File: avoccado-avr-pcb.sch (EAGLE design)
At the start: 31 parts, among them IC1 MCP1703CB, Q1 #MHz, Q2 MOSFET-NCHANNEL2N7002PW, U1 ATMEGA168#, U2 MCP73831, X1 Micro USB

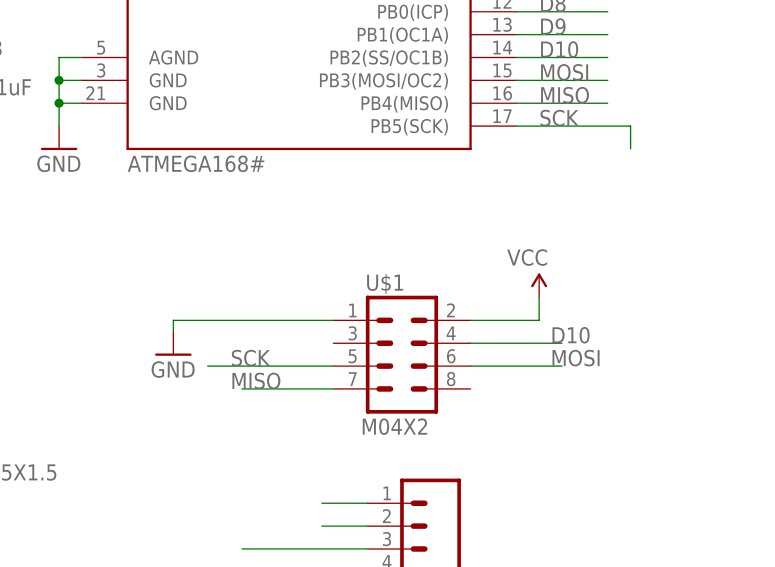
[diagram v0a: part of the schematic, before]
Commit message: route MPU6050 header
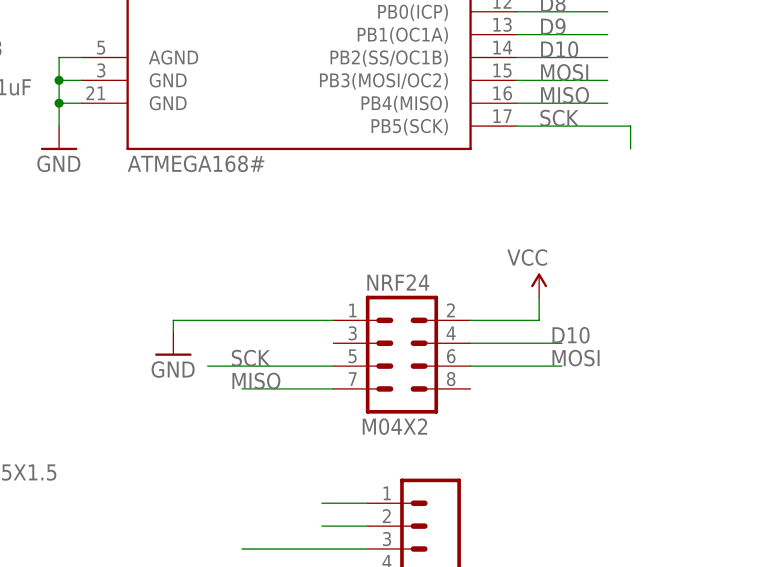
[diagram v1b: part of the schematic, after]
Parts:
- renumbered U$1 to NRF24
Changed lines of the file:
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@@
 <part name="JP10" library="smd-pads" deviceset="M04" device="SMD1X4"/>
 <part name="JP11" library="smd-pads" deviceset="M04" device="SMD1X4"/>
-<part name="U$1" library="SparkFun-Connectors" deviceset="M04X2" device=""/>
+<part name="NRF24" library="SparkFun-Connectors" deviceset="M04X2" device=""/>
 <part name="GND10" library="SparkFun" deviceset="GND" device=""/>
 <part name="P+2" library="SparkFun" deviceset="3.3V" device="" value="VCC"/>
@@
 <instance part="JP10" gate="G$1" x="71.12" y="36.83"/>
 <instance part="JP11" gate="G$1" x="71.12" y="46.99"/>
-<instance part="U$1" gate="G$1" x="203.2" y="69.85"/>
+<instance part="NRF24" gate="G$1" x="203.2" y="69.85"/>
 <instance part="GND10" gate="1" x="177.8" y="71.12"/>
 <instance part="P+2" gate="G$1" x="218.44" y="77.47" smashed="yes">
@@
 </segment>
 <segment>
-<pinref part="U$1" gate="G$1" pin="1"/>
+<pinref part="NRF24" gate="G$1" pin="1"/>
 <wire x1="195.58" y1="74.93" x2="177.8" y2="74.93" width="0.2032" layer="91"/>
 <pinref part="GND10" gate="1" pin="GND"/>
@@
 <segment>
 <wire x1="181.61" y1="69.85" x2="195.58" y2="69.85" width="0.1524" layer="91"/>
-<pinref part="U$1" gate="G$1" pin="5"/>
+<pinref part="NRF24" gate="G$1" pin="5"/>
 <label x="184.15" y="69.85" size="1.778" layer="95"/>
 </segment>
@@
 <segment>
 <wire x1="185.42" y1="67.31" x2="195.58" y2="67.31" width="0.1524" layer="91"/>
-<pinref part="U$1" gate="G$1" pin="7"/>
+<pinref part="NRF24" gate="G$1" pin="7"/>
 <label x="184.15" y="67.31" size="1.778" layer="95"/>
 </segment>
@@
 <segment>
 <wire x1="210.82" y1="69.85" x2="220.98" y2="69.85" width="0.1524" layer="91"/>
-<pinref part="U$1" gate="G$1" pin="6"/>
+<pinref part="NRF24" gate="G$1" pin="6"/>
 <label x="219.71" y="69.85" size="1.778" layer="95"/>
 </segment>
@@
 <segment>
 <wire x1="210.82" y1="72.39" x2="220.98" y2="72.39" width="0.1524" layer="91"/>
-<pinref part="U$1" gate="G$1" pin="4"/>
+<pinref part="NRF24" gate="G$1" pin="4"/>
 <label x="219.71" y="72.39" size="1.778" layer="95"/>
 </segment>
@@
 <pinref part="P+2" gate="G$1" pin="3.3V"/>
 <wire x1="218.44" y1="77.47" x2="218.44" y2="74.93" width="0.2032" layer="91"/>
-<pinref part="U$1" gate="G$1" pin="2"/>
+<pinref part="NRF24" gate="G$1" pin="2"/>
 <wire x1="218.44" y1="74.93" x2="210.82" y2="74.93" width="0.2032" layer="91"/>
 </segment>

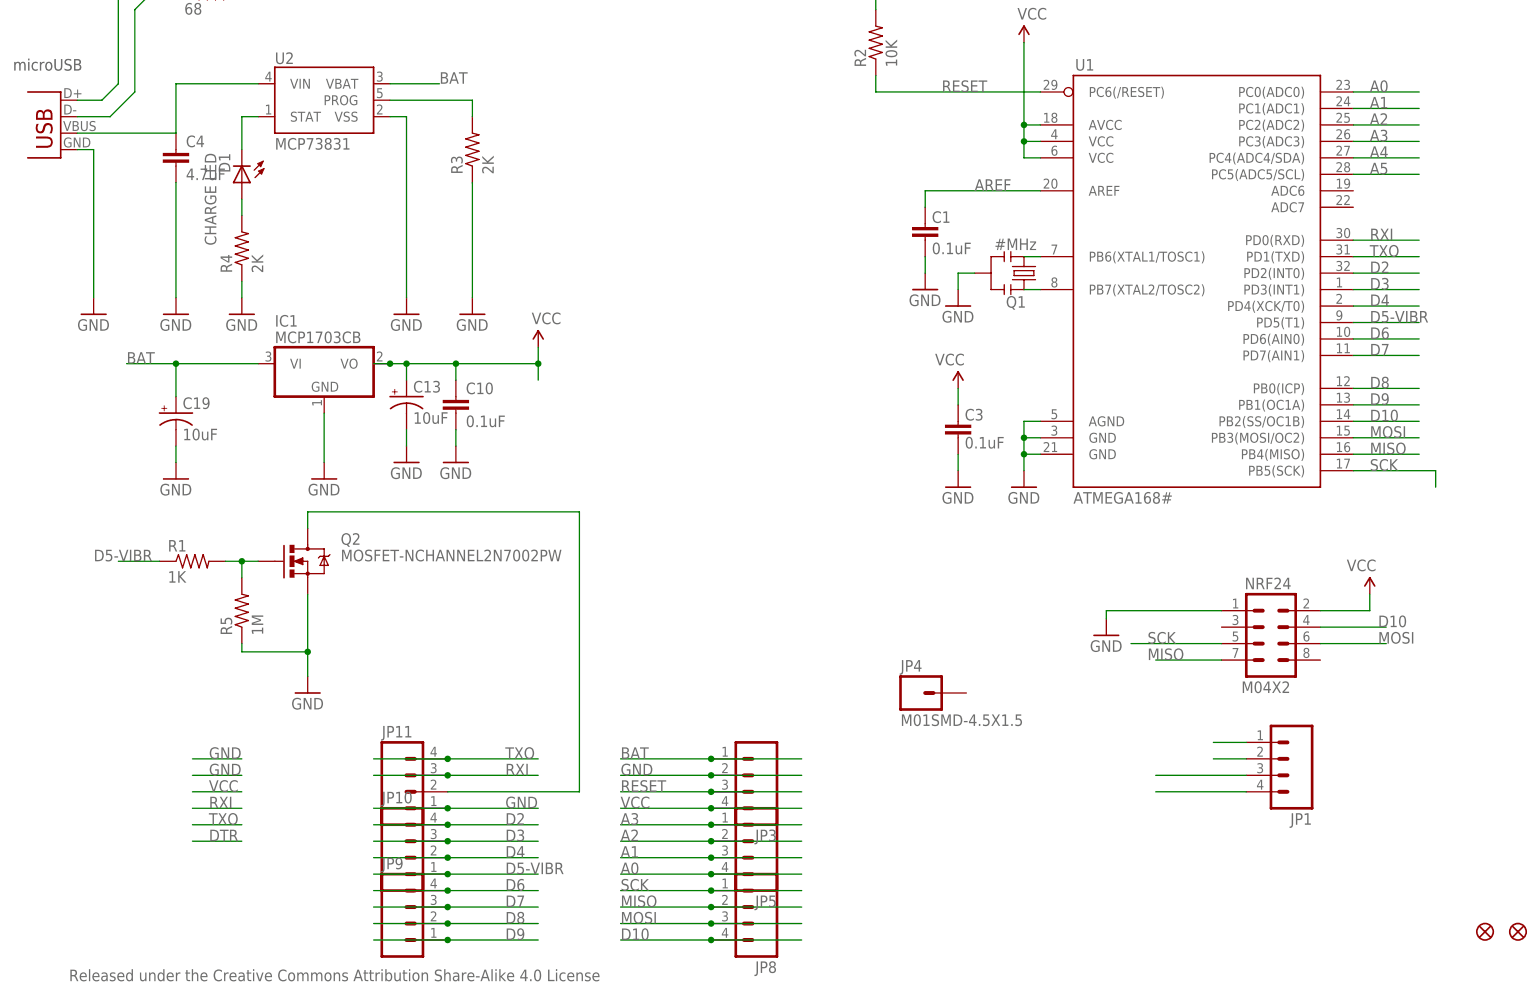
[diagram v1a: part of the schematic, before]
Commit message: rewire filter caps
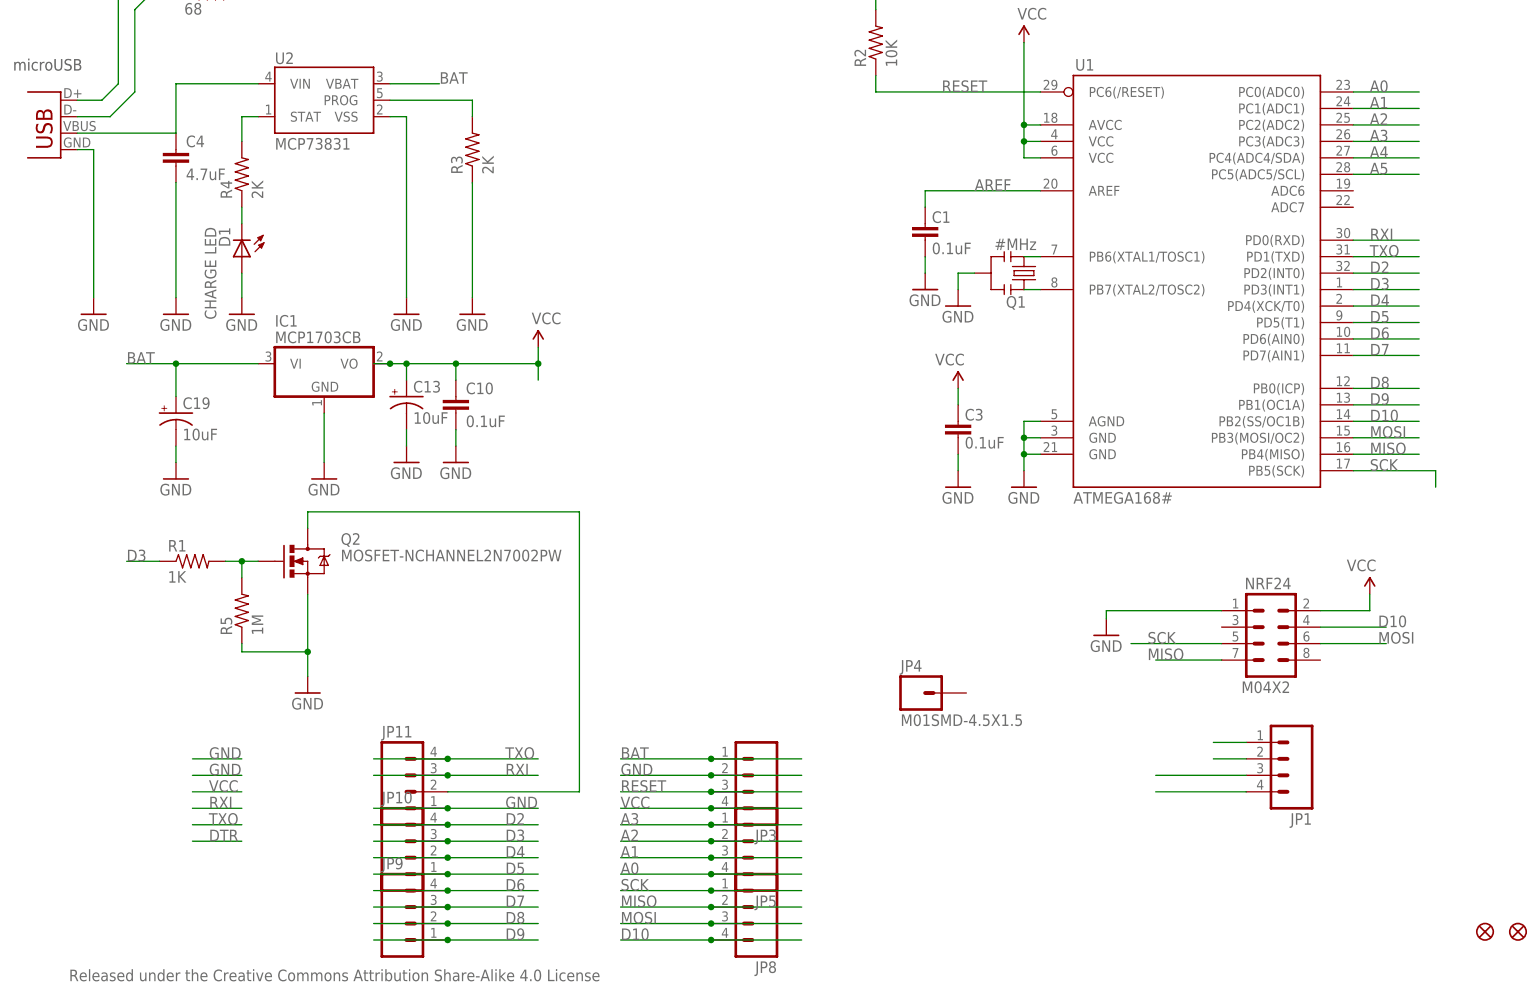
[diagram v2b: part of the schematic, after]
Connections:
- removed net D5-VIBR: JP10.1, R1.1, U1.PD5(T1)
- new net D5: JP10.1, U1.PD5(T1)
- net D3: now also R1.1
- net GND: now also D1.A; no longer R4.1
- net N$4: now also R4.2; no longer D1.C
- net N$5: now also D1.C, R4.1; no longer D1.A, R4.2
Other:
- moved on the sheet: D1, R4
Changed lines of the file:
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@@
 <setting verticaltext="up"/>
 </settings>
-<grid distance="0.05" unitdist="inch" unit="inch" style="lines" multiple="1" display="yes" altdistance="0.01" altunitdist="inch" altunit="inch"/>
+<grid distance="0.05" unitdist="inch" unit="inch" style="lines" multiple="1" display="yes" altdistance="0.005" altunitdist="inch" altunit="inch"/>
 <layers>
 <layer number="1" name="Top" color="4" fill="1" visible="no" active="no"/>
@@
 <instance part="R3" gate="G$1" x="80.01" y="146.05" rot="R90"/>
 <instance part="GND3" gate="1" x="80.01" y="120.65"/>
-<instance part="D1" gate="G$1" x="44.45" y="140.97" rot="R180"/>
+<instance part="D1" gate="G$1" x="44.45" y="129.54" rot="R180"/>
 <instance part="GND15" gate="1" x="21.59" y="120.65"/>
 <instance part="X1" gate="G$1" x="16.51" y="146.05" rot="MR0"/>
 <instance part="C4" gate="G$1" x="34.29" y="143.51"/>
-<instance part="R4" gate="G$1" x="44.45" y="130.81" rot="R90"/>
+<instance part="R4" gate="G$1" x="44.45" y="142.24" rot="R90"/>
 <instance part="GND6" gate="1" x="44.45" y="120.65"/>
 <instance part="GND8" gate="1" x="34.29" y="120.65"/>
@@
 </segment>
 <segment>
-<pinref part="GND6" gate="1" pin="GND"/>
-<pinref part="R4" gate="G$1" pin="1"/>
-<wire x1="44.45" y1="123.19" x2="44.45" y2="125.73" width="0.1524" layer="91"/>
-</segment>
-<segment>
 <pinref part="C4" gate="G$1" pin="2"/>
 <pinref part="GND8" gate="1" pin="GND"/>
@@
 <wire x1="199.39" y1="54.61" x2="194.31" y2="54.61" width="0.1524" layer="91"/>
 <pinref part="JP1" gate="G$1" pin="1"/>
+</segment>
+<segment>
+<pinref part="GND6" gate="1" pin="GND"/>
+<wire x1="44.45" y1="123.19" x2="44.45" y2="127" width="0.1524" layer="91"/>
+<pinref part="D1" gate="G$1" pin="A"/>
 </segment>
 </net>
@@
 <wire x1="76.2" y1="39.37" x2="64.77" y2="39.37" width="0.1524" layer="91"/>
 <junction x="76.2" y="39.37"/>
+<label x="26.67" y="82.55" size="1.778" layer="95"/>
 </segment>
 <segment>
@@
 <label x="218.44" y="124.46" size="1.778" layer="95"/>
 <pinref part="U1" gate="G$1" pin="PD3(INT1)"/>
+</segment>
+<segment>
+<pinref part="R1" gate="G$1" pin="1"/>
+<wire x1="31.75" y1="82.55" x2="26.67" y2="82.55" width="0.1524" layer="91"/>
 </segment>
 </net>
@@
 </segment>
 </net>
-<net name="D5-VIBR" class="0">
+<net name="D5" class="0">
 <segment>
 <label x="85.09" y="34.29" size="1.778" layer="95"/>
@@
 <label x="218.44" y="119.38" size="1.778" layer="95"/>
 <pinref part="U1" gate="G$1" pin="PD5(T1)"/>
-</segment>
-<segment>
-<pinref part="R1" gate="G$1" pin="1"/>
-<wire x1="31.75" y1="82.55" x2="25.4" y2="82.55" width="0.1524" layer="91"/>
-<label x="21.59" y="82.55" size="1.778" layer="95"/>
 </segment>
 </net>
@@
 <segment>
 <pinref part="U2" gate="G$1" pin="STAT"/>
-<pinref part="D1" gate="G$1" pin="C"/>
 <wire x1="46.99" y1="151.13" x2="44.45" y2="151.13" width="0.1524" layer="91"/>
-<wire x1="44.45" y1="151.13" x2="44.45" y2="146.05" width="0.1524" layer="91"/>
-</segment>
-</net>
-<net name="N$5" class="0">
-<segment>
 <pinref part="R4" gate="G$1" pin="2"/>
-<pinref part="D1" gate="G$1" pin="A"/>
-<wire x1="44.45" y1="135.89" x2="44.45" y2="138.43" width="0.1524" layer="91"/>
+<wire x1="44.45" y1="147.32" x2="44.45" y2="151.13" width="0.1524" layer="91"/>
 </segment>
 </net>
@@
 </segment>
 </net>
+<net name="N$5" class="0">
+<segment>
+<pinref part="D1" gate="G$1" pin="C"/>
+<pinref part="R4" gate="G$1" pin="1"/>
+<wire x1="44.45" y1="134.62" x2="44.45" y2="137.16" width="0.1524" layer="91"/>
+</segment>
+</net>
